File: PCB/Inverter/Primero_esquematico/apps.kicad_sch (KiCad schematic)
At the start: 24 parts, among them J6 347928082, U39 OPA2196xD, U40 TLV1701AQDCKRQ1

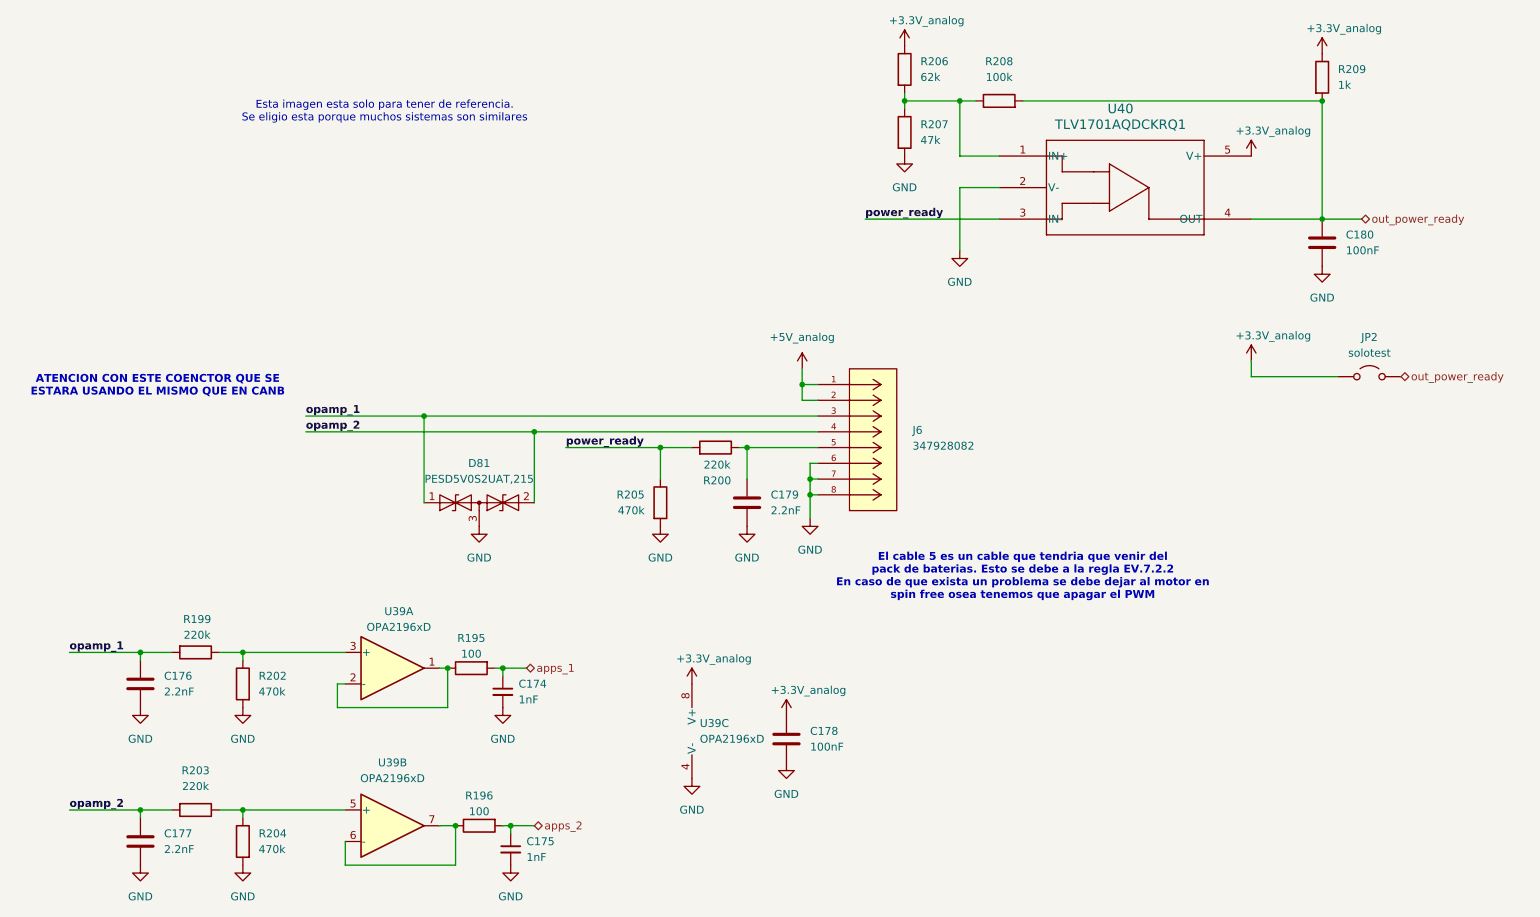
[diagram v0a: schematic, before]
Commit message: EsqumaticoCuasifinalizado
Ya hice varias correcciones creo q solo falta cambiar algunas resistencias en los limites q tendrian que estar en el notion
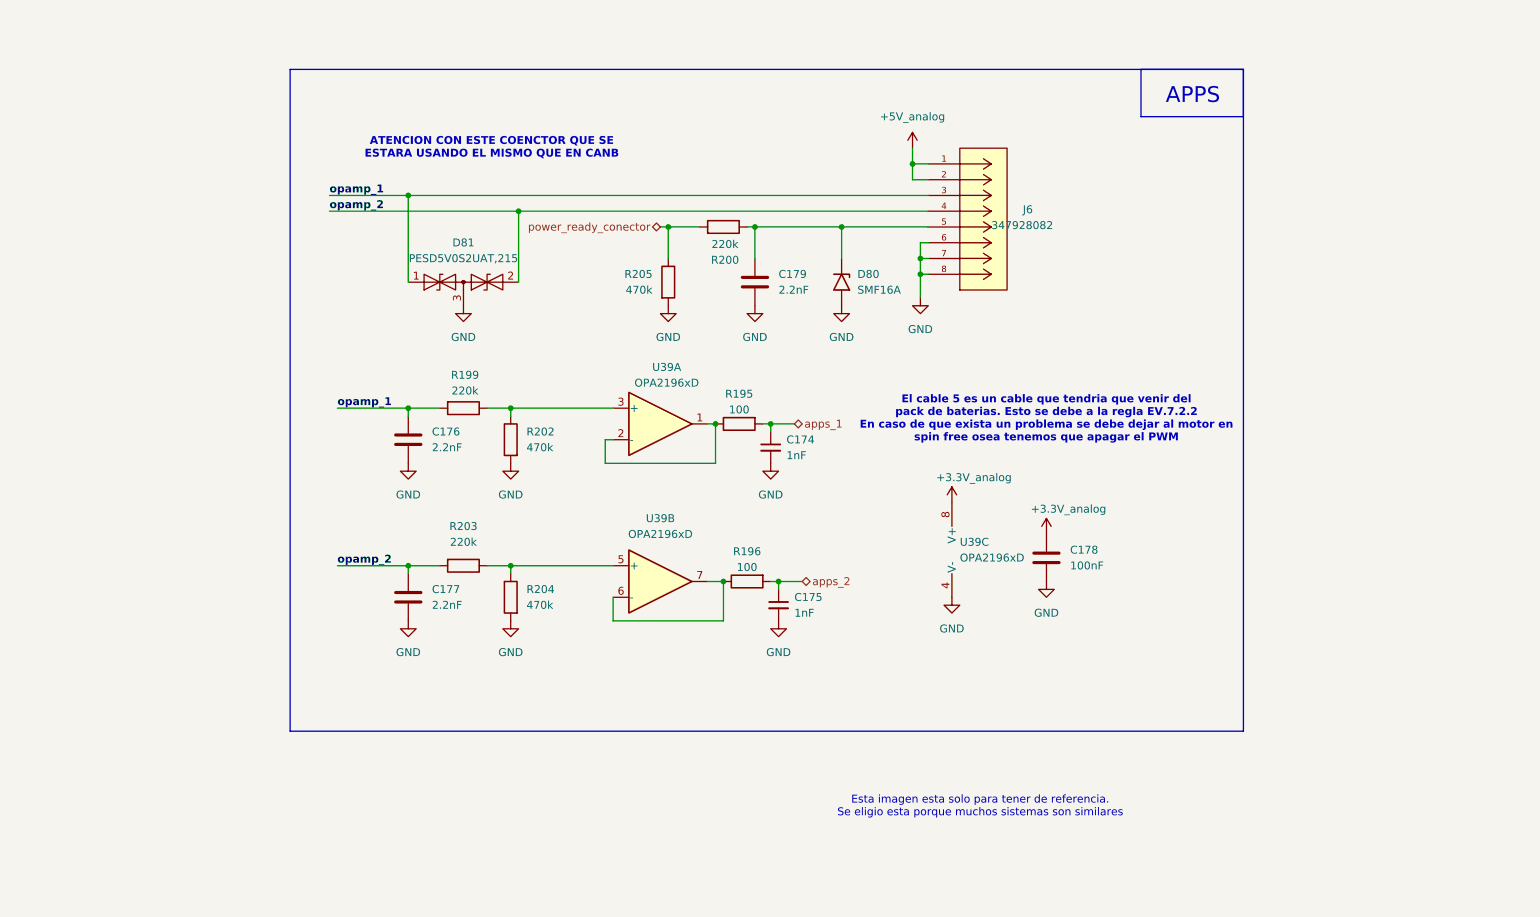
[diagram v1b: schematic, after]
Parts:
- removed C180: 100nF, Capacitor_SMD:C_0402_1005Metric, symbol Device:C
- removed JP2: solotest, Jumper:SolderJumper-2_P1.3mm_Open_RoundedPad1.0x1.5mm, symbol Jumper:Jumper_2_Open
- removed R206: 62k, Resistor_SMD:R_0402_1005Metric, symbol Device:R
- removed R207: 47k, Resistor_SMD:R_0402_1005Metric, symbol Device:R
- removed R208: 100k, Resistor_SMD:R_0402_1005Metric, symbol Device:R
- removed R209: 1k, Resistor_SMD:R_0402_1005Metric, symbol Device:R
- removed U40: TLV1701AQDCKRQ1, Snapeda:SOIC_DCKRQ1_TEX-L, symbol Snapeda:TLV1701AQDCKRQ1
- added D80: SMF16A, Diode_SMD:D_SMF, symbol Diode:SMF16A
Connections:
- net GND: now also D80.2 (A2)
- net at C179.2, J6.5, R200.1: now also D80.1 (A1)
- net power_ready renamed power_ready_conector
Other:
- note added: "APPS"
- moved on the sheet: C174, C175, C176, C177, C178, C179, D81, J6, R195, R196, R199, R200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

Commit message: Modificaciones por falta de stock
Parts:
- added D86: SMF16A, Diode_SMD:D_SMF, symbol Diode:SMF16A
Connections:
- net +5V_analog: now also D86.1 (A1)
- net GND: now also D86.2 (A2)
